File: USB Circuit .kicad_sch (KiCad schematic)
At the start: 13 parts, among them J1 USB_C_Receptacle, U1 VL162

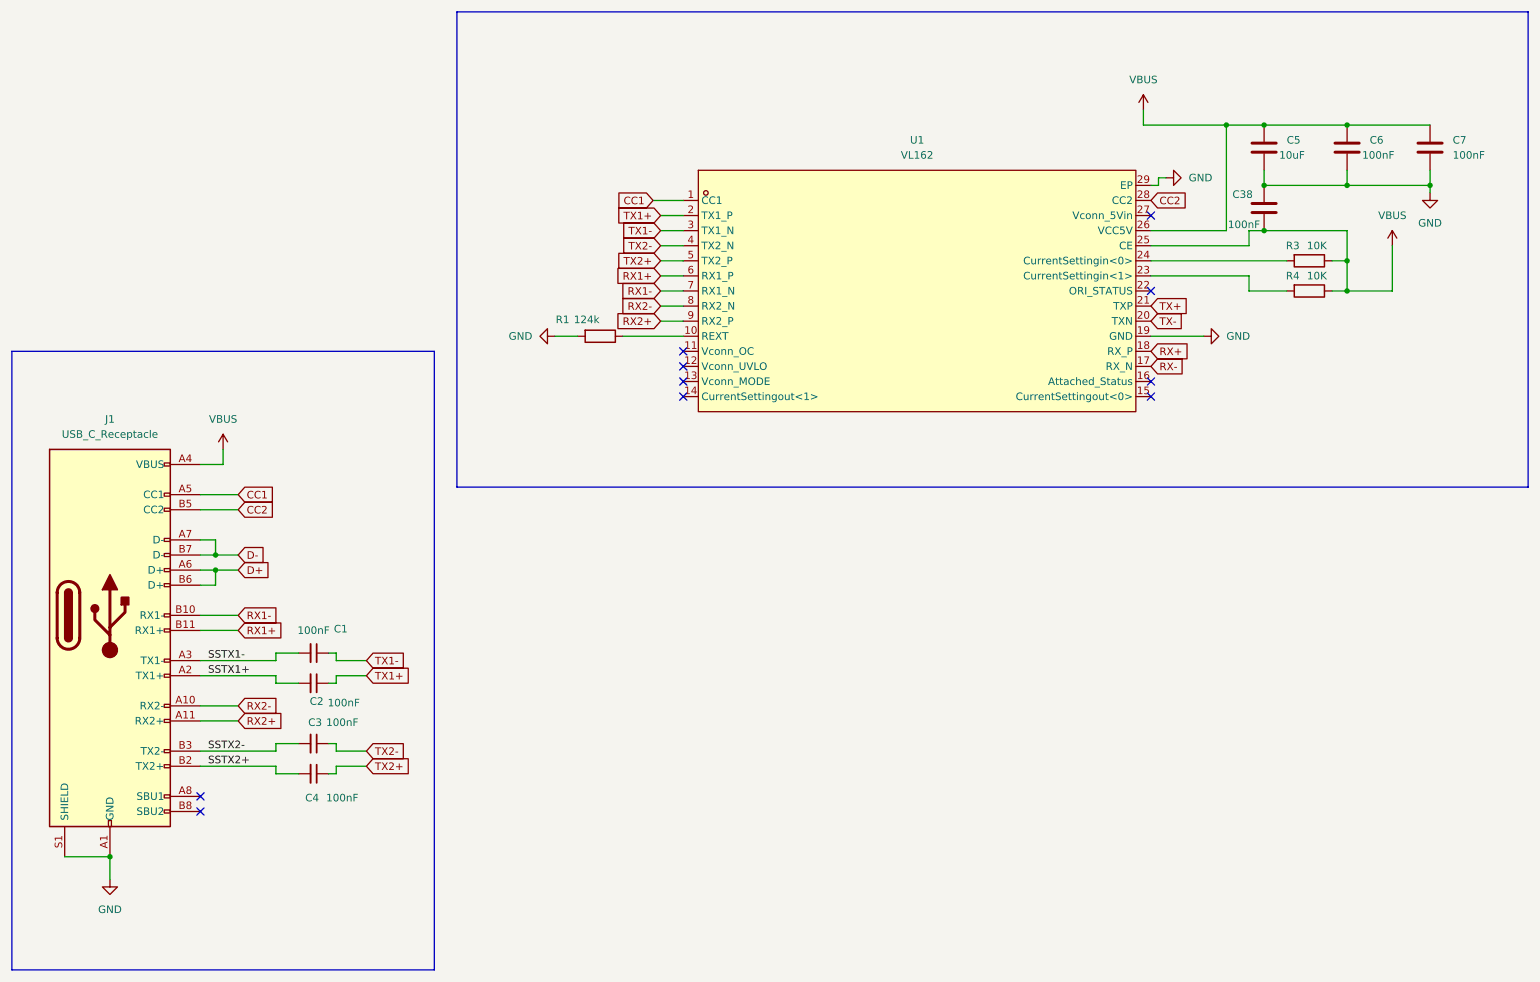
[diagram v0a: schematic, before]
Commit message: Fixed usb footprint
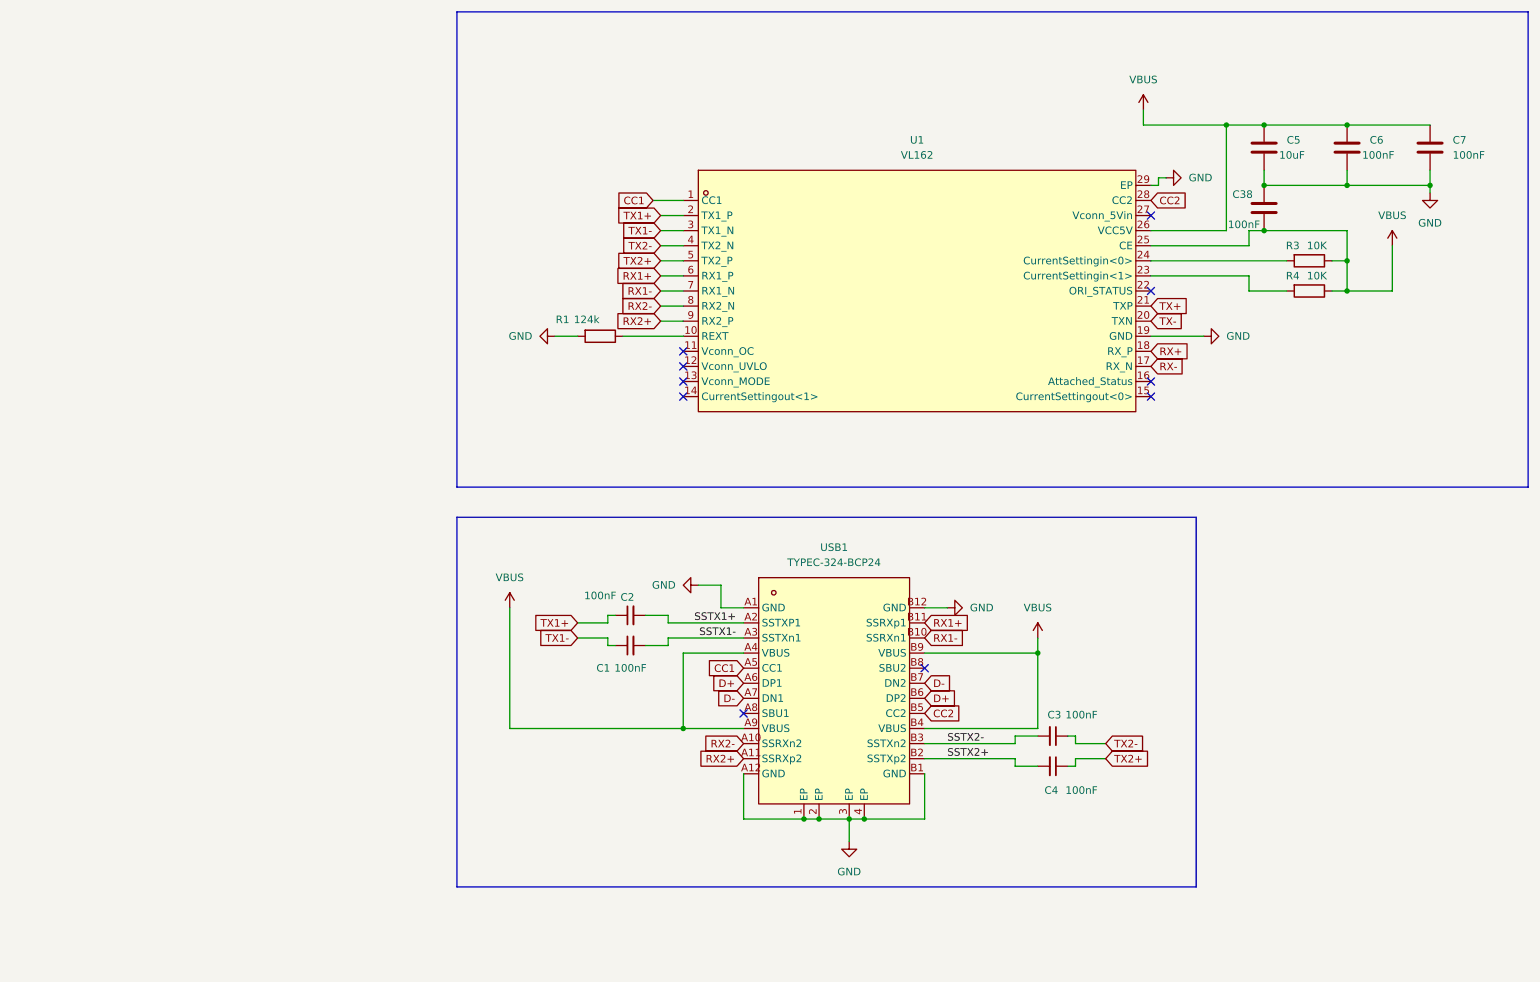
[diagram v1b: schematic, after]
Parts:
- removed J1: USB_C_Receptacle, Connector_USB:USB_C_Receptacle_Amphenol_12401548E4-2A, symbol Connector:USB_C_Receptacle
- added USB1: TYPEC-324-BCP24, da:USB-C-SMD_TYPEC-324-BCP24, symbol da:TYPEC-324-BCP24
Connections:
- net CC1: now also USB1.A5 (CC1)
- net CC2: now also USB1.B5 (CC2)
- net D+: now also USB1.A6 (DP1), USB1.B6 (DP2)
- net D-: now also USB1.A7 (DN1), USB1.B7 (DN2)
- net GND: now also USB1.1 (EP), USB1.2 (EP), USB1.3 (EP), USB1.4 (EP), USB1.A1 (GND), USB1.A12 (GND), USB1.B1 (GND), USB1.B12 (GND)
- net RX1+: now also USB1.B11 (SSRXp1)
- net RX1-: now also USB1.B10 (SSRXn1)
- net RX2+: now also USB1.A11 (SSRXp2)
- net RX2-: now also USB1.A10 (SSRXn2)
- net SSTX1+: now also USB1.A2 (SSTXP1)
- net SSTX1-: now also USB1.A3 (SSTXn1)
- net SSTX2+: now also USB1.B2 (SSTXp2)
- net SSTX2-: now also USB1.B3 (SSTXn2)
- net VBUS: now also USB1.A4 (VBUS), USB1.A9 (VBUS), USB1.B4 (VBUS), USB1.B9 (VBUS)
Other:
- moved on the sheet: C3, C4
